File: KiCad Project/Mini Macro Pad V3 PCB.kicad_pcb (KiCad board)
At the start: 4 copper layers, 65 x 65 mm, 99 parts, among them J1 USB_C_Receptacle_USB2.0_14P, SW1 SW_Push bootsel, SW10 SW_Push, SW11 SW_Push, SW12 SW_Push, SW13 SW_Push, SW14 SW_Push, SW15 SW_Push, SW16 SW_Push, SW17 SW_Push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

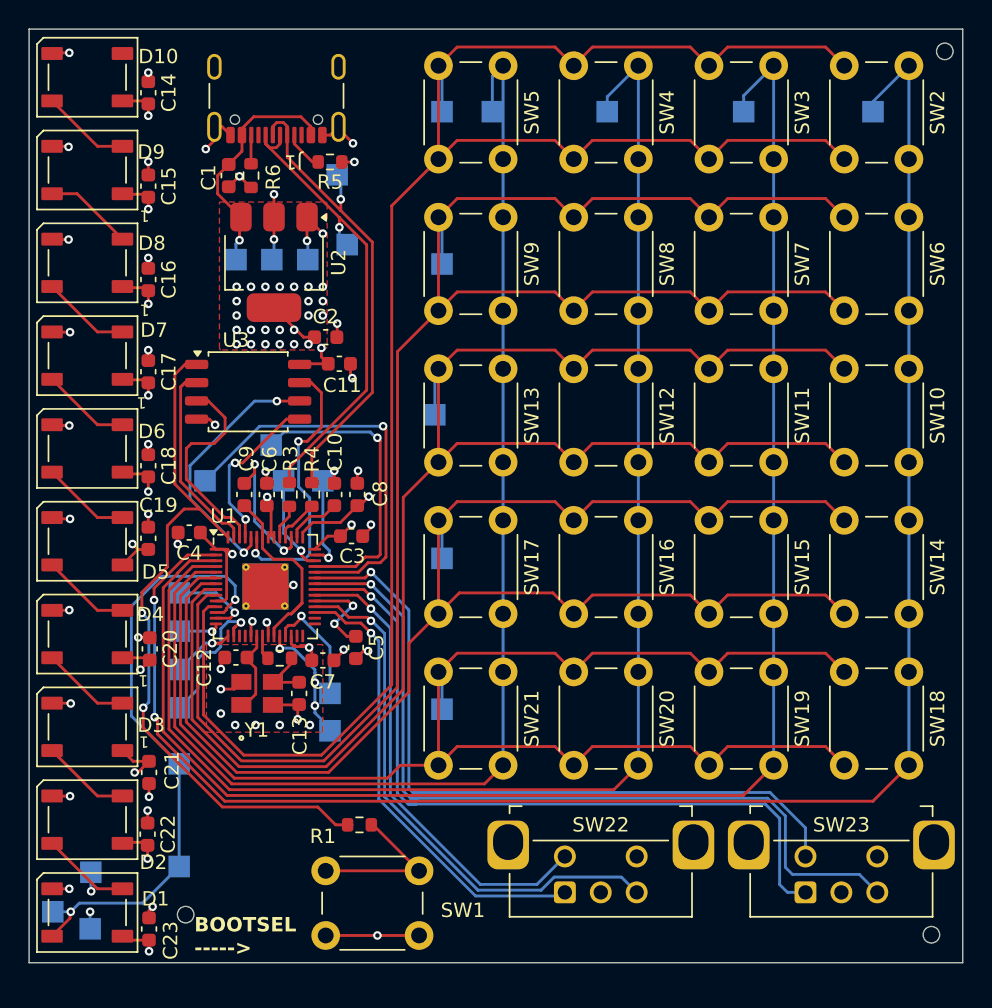
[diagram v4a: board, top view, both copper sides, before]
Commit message: Replaced all micro vias with through vias
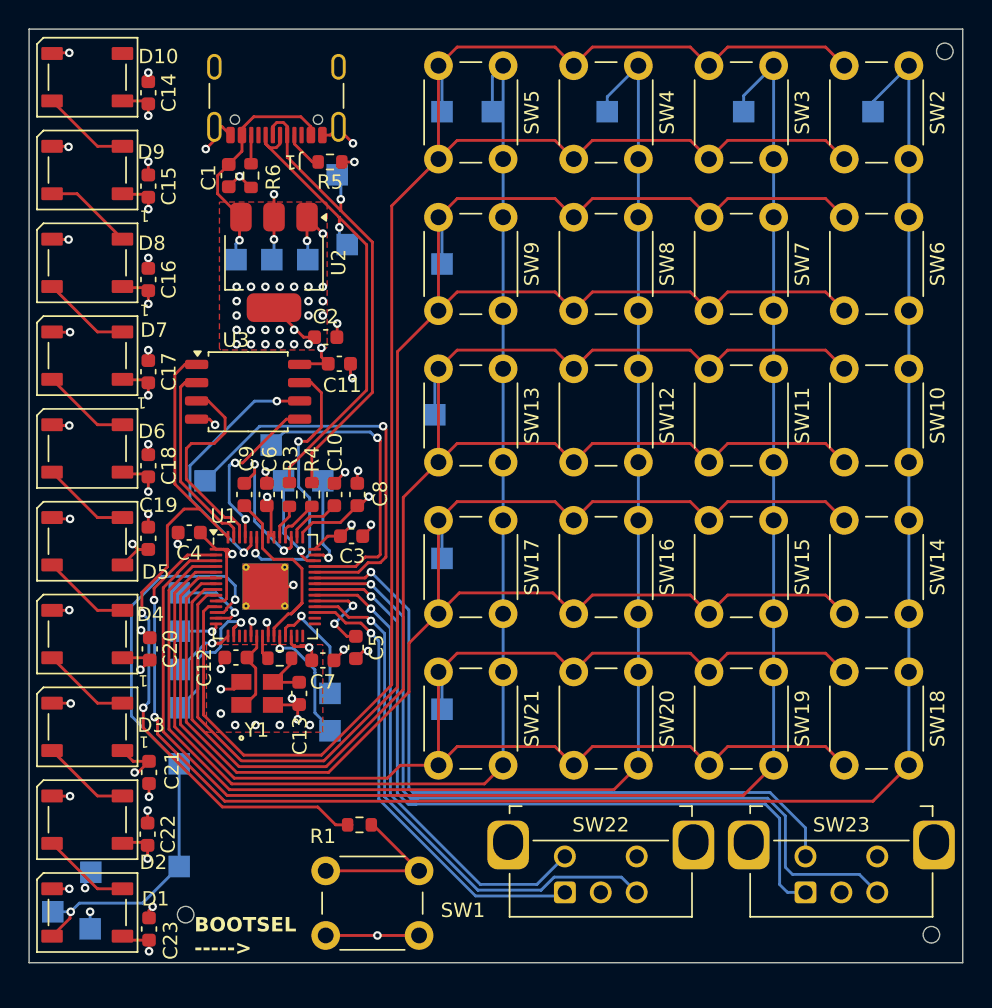
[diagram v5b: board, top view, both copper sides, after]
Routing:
- net +3.3V: track 70.9 -> 71.8 mm
- net GND: track 58.6 -> 59.1 mm, vias 49 -> 48

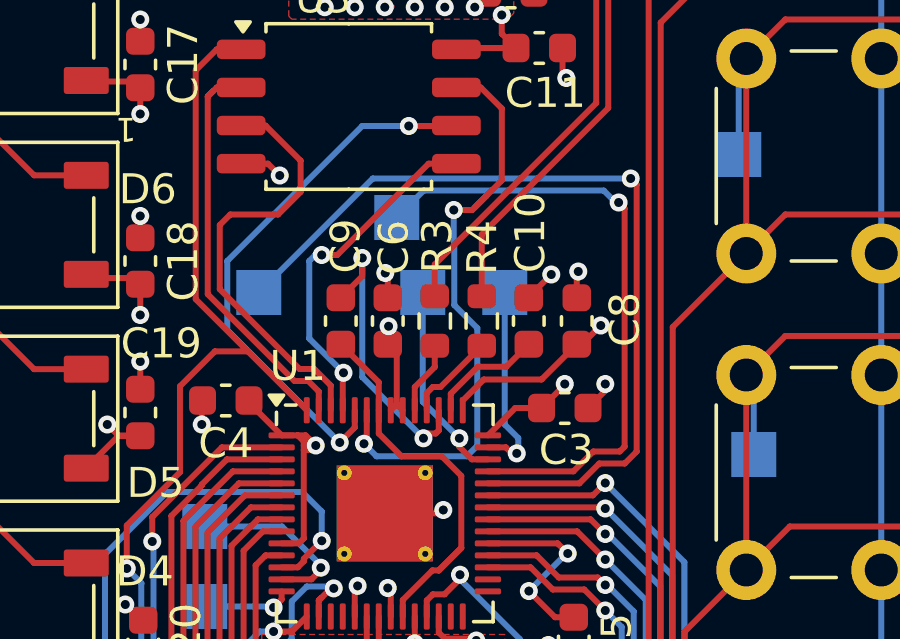
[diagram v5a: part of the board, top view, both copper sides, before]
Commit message: changed PCB to reflect changes in schematic
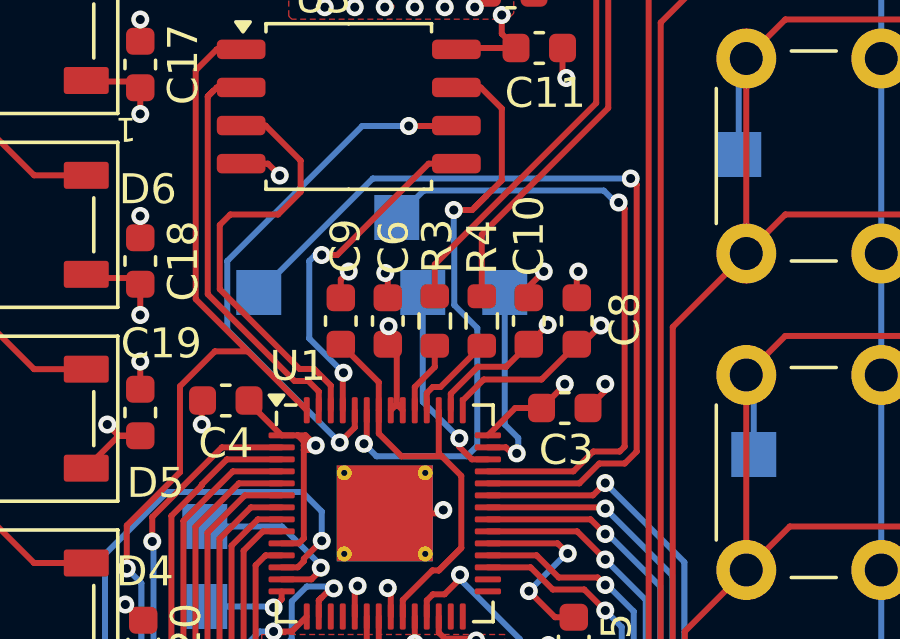
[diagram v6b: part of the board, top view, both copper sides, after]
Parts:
- turned C10 to 90 degrees
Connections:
- C10 pad 2: Net-(U1-VREG_IN) -> GND
- C9 pad 1: Net-(C9-Pad1) -> Net-(U1-VREG_VOUT)
- C9 pad 2: Net-(U1-VREG_VOUT) -> GND
- U1 pad 23: Net-(C9-Pad1) -> Net-(U1-VREG_VOUT)
- U1 pad 44: Net-(U1-VREG_IN) -> +3.3V
- U1 pad 50: Net-(C9-Pad1) -> Net-(U1-VREG_VOUT)
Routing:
- net Net-(C9-Pad1): track 13.5 -> 0.00 mm
- net Net-(U1-VREG_VOUT): track 9.77 -> 15.1 mm, vias 2 -> 0
- net Net-(U1-VREG_IN): track 3.83 -> 0.00 mm
- net +3.3V: track 71.8 -> 75.4 mm
- net GND: track 59.1 -> 61.3 mm, vias 48 -> 50
